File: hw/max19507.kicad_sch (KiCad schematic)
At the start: 43 parts, among them U8 THS4522, U9 MAX19517

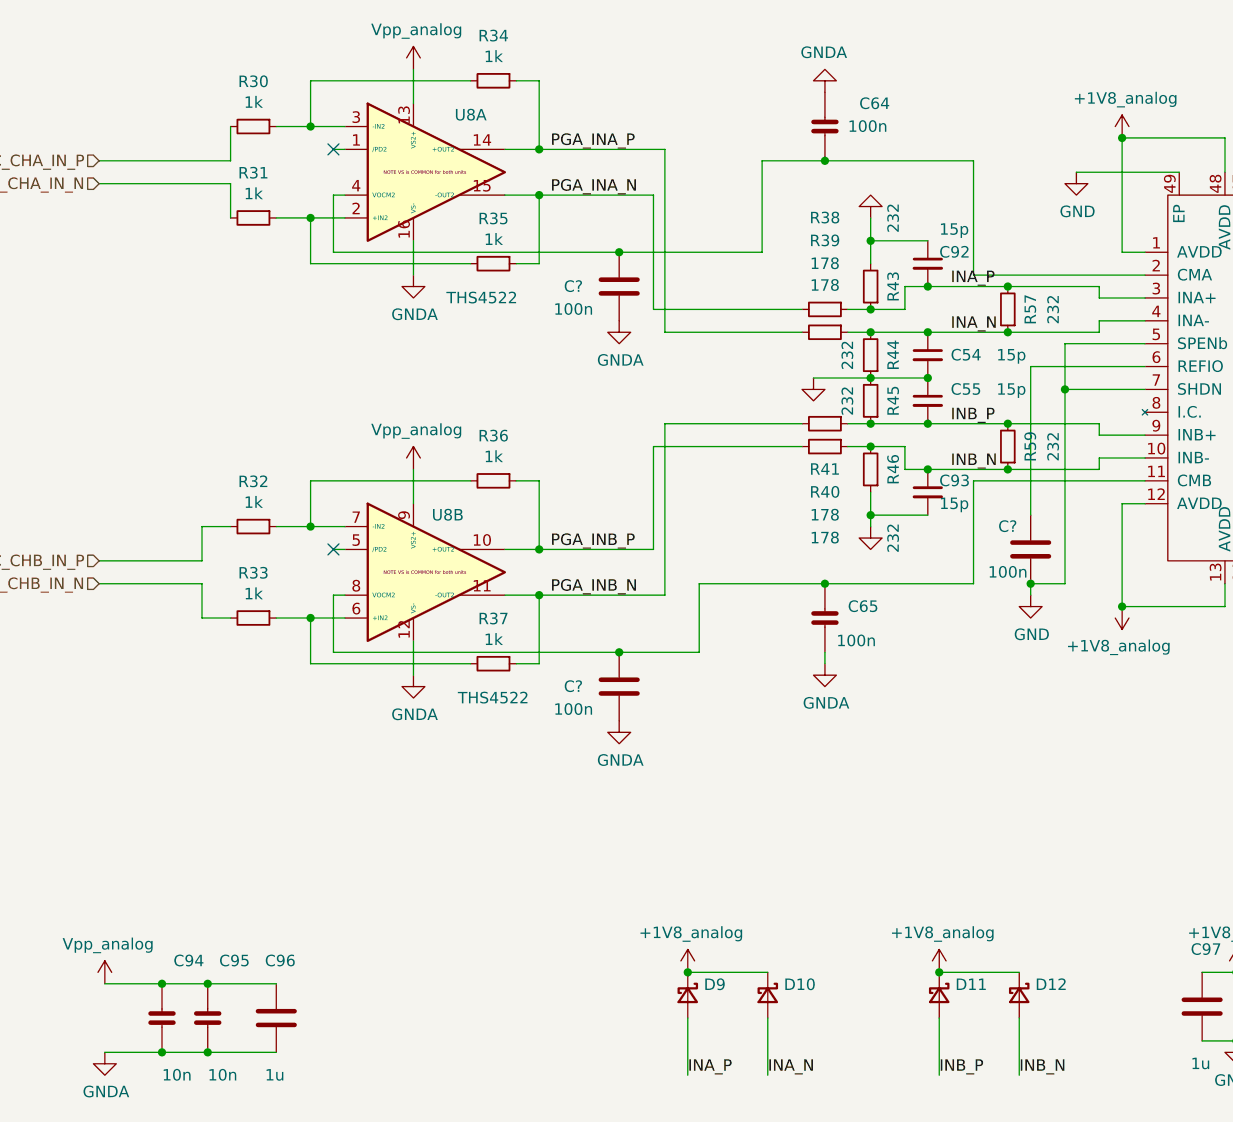
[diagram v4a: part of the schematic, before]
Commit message: standardized resistor/capacitor values
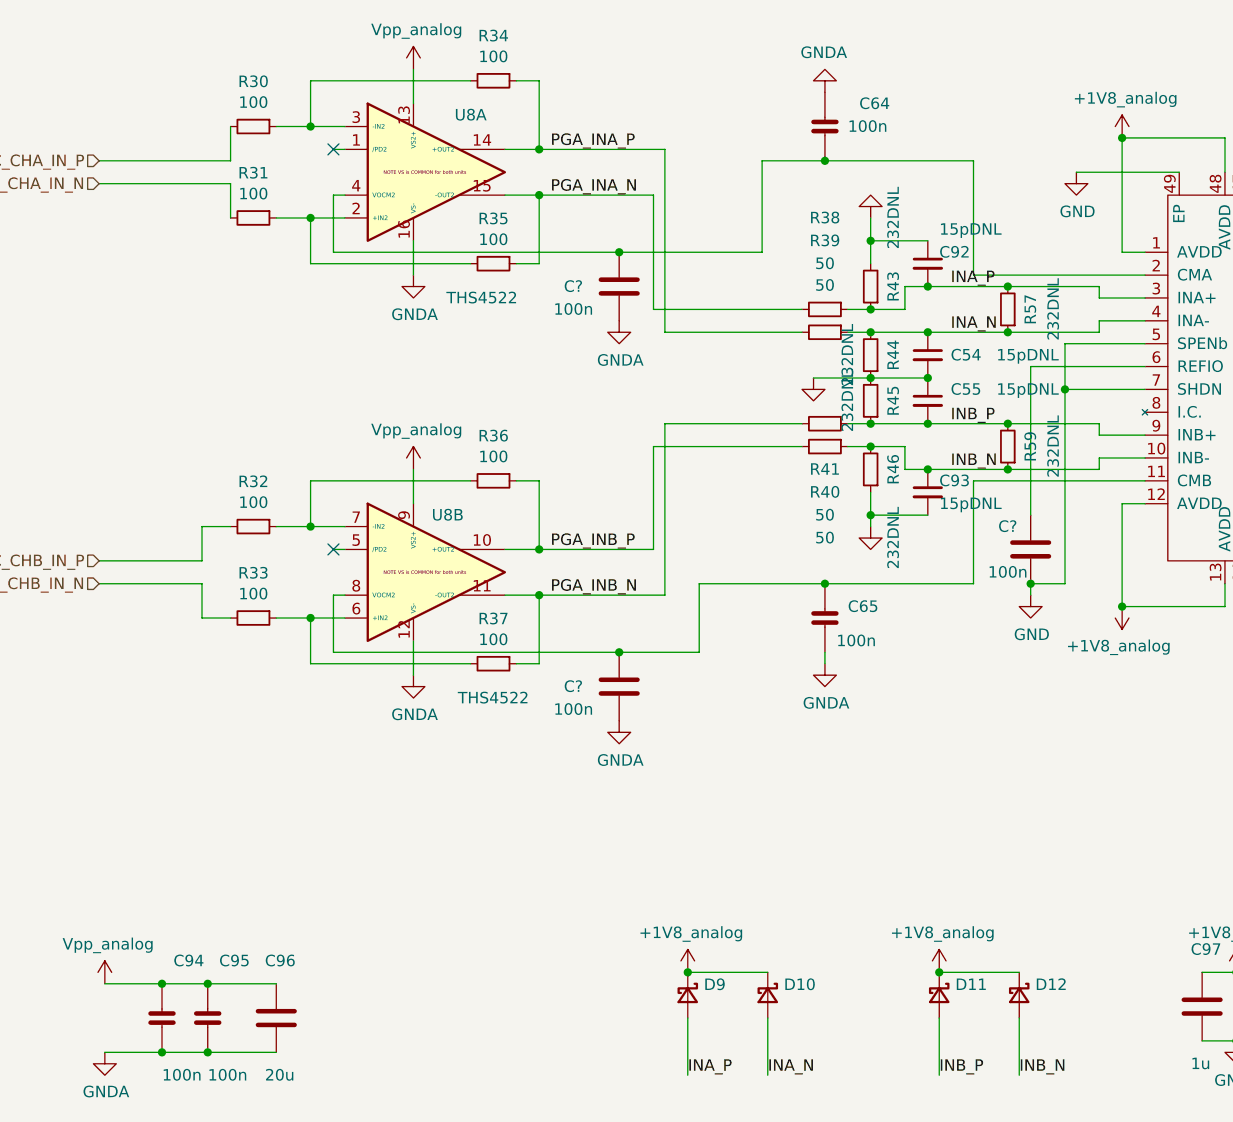
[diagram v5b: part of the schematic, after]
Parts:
- C54, C55, C92, C93: value 15p -> 15pDNL
- C94, C95: value 10n -> 100n
- C96: value 1u -> 20u
- R30, R31, R32, R33, R34, R35, R36, R37: value 1k -> 100
- R38, R39, R40, R41: value 178 -> 50
- R43, R44, R45, R46, R57, R59: value 232 -> 232DNL
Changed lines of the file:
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@@
       (effects (font (size 1.27 1.27)))
     )
-    (property "Value" "232" (at 191.77 78.74 90)
+    (property "Value" "232DNL" (at 191.77 78.74 90)
       (effects (font (size 1.27 1.27)))
     )
@@
       (effects (font (size 1.27 1.27)))
     )
-    (property "Value" "232" (at 191.77 93.98 90)
+    (property "Value" "232DNL" (at 191.77 93.98 90)
       (effects (font (size 1.27 1.27)))
     )
@@
       (effects (font (size 1.27 1.27)) (justify left))
     )
-    (property "Value" "15p" (at 179.07 100.33 0)
+    (property "Value" "15pDNL" (at 179.07 100.33 0)
       (effects (font (size 1.27 1.27)) (justify left))
     )
@@
       (effects (font (size 1.27 1.27)) (justify left))
     )
-    (property "Value" "15p" (at 179.07 69.85 0)
+    (property "Value" "15pDNL" (at 179.07 69.85 0)
       (effects (font (size 1.27 1.27)) (justify left))
     )
@@
       (effects (font (size 1.27 1.27)) (justify left))
     )
-    (property "Value" "10n" (at 92.71 163.83 0)
+    (property "Value" "100n" (at 92.71 163.83 0)
       (effects (font (size 1.27 1.27)) (justify left))
     )
@@
       (effects (font (size 1.27 1.27)) (justify left))
     )
-    (property "Value" "10n" (at 97.79 163.83 0)
+    (property "Value" "100n" (at 97.79 163.83 0)
       (effects (font (size 1.27 1.27)) (justify left))
     )
@@
       (effects (font (size 1.27 1.27)) (justify left))
     )
-    (property "Value" "1u" (at 104.14 163.83 0)
+    (property "Value" "20u" (at 104.14 163.83 0)
       (effects (font (size 1.27 1.27)) (justify left))
     )
@@
       (effects (font (size 1.27 1.27)))
     )
-    (property "Value" "232" (at 168.91 83.82 90)
+    (property "Value" "232DNL" (at 168.91 83.82 90)
       (effects (font (size 1.27 1.27)))
     )
@@
       (effects (font (size 1.27 1.27)))
     )
-    (property "Value" "232" (at 173.99 68.58 90)
+    (property "Value" "232DNL" (at 173.99 68.58 90)
       (effects (font (size 1.27 1.27)))
     )
@@
       (effects (font (size 1.27 1.27)))
     )
-    (property "Value" "232" (at 168.91 88.9 90)
+    (property "Value" "232DNL" (at 168.91 88.9 90)
       (effects (font (size 1.27 1.27)))
     )
@@
       (effects (font (size 1.27 1.27)))
     )
-    (property "Value" "232" (at 173.99 104.14 90)
+    (property "Value" "232DNL" (at 173.99 104.14 90)
       (effects (font (size 1.27 1.27)))
     )
@@
       (effects (font (size 1.27 1.27)))
     )
-    (property "Value" "178" (at 166.37 76.073 90)
+    (property "Value" "50" (at 166.37 76.073 90)
       (effects (font (size 1.27 1.27)))
     )
@@
       (effects (font (size 1.27 1.27)) (justify left))
     )
-    (property "Value" "15p" (at 185.42 83.82 0)
+    (property "Value" "15pDNL" (at 185.42 83.82 0)
       (effects (font (size 1.27 1.27)) (justify left))
     )
@@
       (effects (font (size 1.27 1.27)))
     )
-    (property "Value" "178" (at 166.37 73.66 90)
+    (property "Value" "50" (at 166.37 73.66 90)
       (effects (font (size 1.27 1.27)))
     )
@@
       (effects (font (size 1.27 1.27)))
     )
-    (property "Value" "1k" (at 129.54 50.673 90)
+    (property "Value" "100" (at 129.54 50.673 90)
       (effects (font (size 1.27 1.27)))
     )
@@
       (effects (font (size 1.27 1.27)))
     )
-    (property "Value" "1k" (at 102.87 55.753 90)
+    (property "Value" "100" (at 102.87 55.753 90)
       (effects (font (size 1.27 1.27)))
     )
@@
       (effects (font (size 1.27 1.27)))
     )
-    (property "Value" "1k" (at 102.87 65.913 90)
+    (property "Value" "100" (at 102.87 65.913 90)
       (effects (font (size 1.27 1.27)))
     )
@@
       (effects (font (size 1.27 1.27)))
     )
-    (property "Value" "1k" (at 129.54 70.993 90)
+    (property "Value" "100" (at 129.54 70.993 90)
       (effects (font (size 1.27 1.27)))
     )
@@
       (effects (font (size 1.27 1.27)))
     )
-    (property "Value" "178" (at 166.37 104.14 90)
+    (property "Value" "50" (at 166.37 104.14 90)
       (effects (font (size 1.27 1.27)))
     )
@@
       (effects (font (size 1.27 1.27)) (justify left))
     )
-    (property "Value" "15p" (at 185.42 87.63 0)
+    (property "Value" "15pDNL" (at 185.42 87.63 0)
       (effects (font (size 1.27 1.27)) (justify left))
     )
@@
       (effects (font (size 1.27 1.27)))
     )
-    (property "Value" "178" (at 166.37 101.6 90)
+    (property "Value" "50" (at 166.37 101.6 90)
       (effects (font (size 1.27 1.27)))
     )
@@
       (effects (font (size 1.27 1.27)))
     )
-    (property "Value" "1k" (at 129.54 95.123 90)
+    (property "Value" "100" (at 129.54 95.123 90)
       (effects (font (size 1.27 1.27)))
     )
@@
       (effects (font (size 1.27 1.27)))
     )
-    (property "Value" "1k" (at 102.87 100.203 90)
+    (property "Value" "100" (at 102.87 100.203 90)
       (effects (font (size 1.27 1.27)))
     )
@@
       (effects (font (size 1.27 1.27)))
     )
-    (property "Value" "1k" (at 102.87 110.363 90)
+    (property "Value" "100" (at 102.87 110.363 90)
       (effects (font (size 1.27 1.27)))
     )
@@
       (effects (font (size 1.27 1.27)))
     )
-    (property "Value" "1k" (at 129.54 115.443 90)
-      (effects (font (size 1.27 1.27)))
-    )
+    (property "Value" "100" (at 129.54 115.443 90)
+      (effects (font (size 1.27 1.27)))
+    )

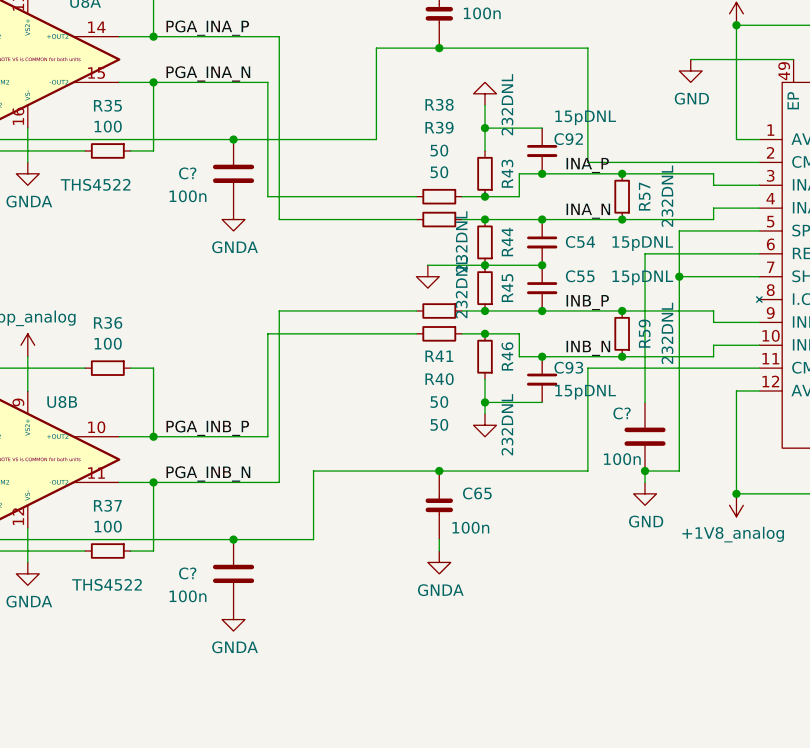
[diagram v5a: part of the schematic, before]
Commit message: Added trion top-sheet as sub-sheet to usbadc project
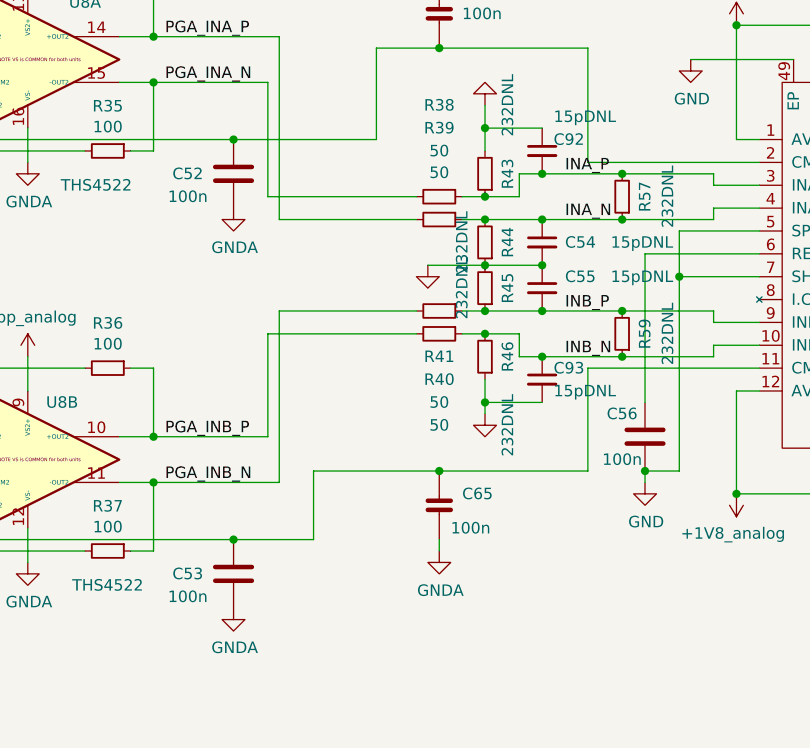
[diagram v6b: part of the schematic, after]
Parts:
- gave numbers to parts that had none: 3
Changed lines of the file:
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@@
           (reference "#PWR0145") (unit 1)
-        )
-        (path "/7c8a1f8d-8834-4c9b-aaae-1f231e9b09a1/00000000-0000-0000-0000-000060b16d71"
-          (reference "#PWR?") (unit 1)
-        )
-        (path "/7c8a1f8d-8834-4c9b-aaae-1f231e9b09a1/00000000-0000-0000-0000-00006086f2e3"
-          (reference "#PWR?") (unit 1)
         )
       )
@@
           (reference "C96") (unit 1)
         )
-        (path "/7c8a1f8d-8834-4c9b-aaae-1f231e9b09a1/00000000-0000-0000-0000-000060b16d71"
-          (reference "C?") (unit 1)
-        )
       )
     )
@@
           (reference "C97") (unit 1)
         )
-        (path "/7c8a1f8d-8834-4c9b-aaae-1f231e9b09a1/00000000-0000-0000-0000-000060b16d71"
-          (reference "C?") (unit 1)
-        )
       )
     )
@@
           (reference "#PWR0148") (unit 1)
         )
-        (path "/7c8a1f8d-8834-4c9b-aaae-1f231e9b09a1/00000000-0000-0000-0000-000060b16d71"
-          (reference "#PWR?") (unit 1)
-        )
-        (path "/7c8a1f8d-8834-4c9b-aaae-1f231e9b09a1/00000000-0000-0000-0000-00006086f2e3"
-          (reference "#PWR?") (unit 1)
-        )
       )
     )
@@
           (reference "#PWR0139") (unit 1)
         )
-        (path "/7c8a1f8d-8834-4c9b-aaae-1f231e9b09a1/00000000-0000-0000-0000-000060b16d71"
-          (reference "#PWR?") (unit 1)
-        )
-        (path "/7c8a1f8d-8834-4c9b-aaae-1f231e9b09a1/00000000-0000-0000-0000-00006086f2e3"
-          (reference "#PWR?") (unit 1)
-        )
       )
     )
@@
         (path "/7c8a1f8d-8834-4c9b-aaae-1f231e9b09a1/00000000-0000-0000-0000-0000612b1274"
           (reference "#PWR0122") (unit 1)
-        )
-        (path "/7c8a1f8d-8834-4c9b-aaae-1f231e9b09a1/00000000-0000-0000-0000-000060b16d71"
-          (reference "#PWR?") (unit 1)
-        )
-        (path "/7c8a1f8d-8834-4c9b-aaae-1f231e9b09a1/00000000-0000-0000-0000-00006086f2e3"
-          (reference "#PWR?") (unit 1)
         )
       )
@@
   (symbol (lib_id "fmc:100nF_603") (at 143.51 76.2 180) (unit 1)
     (in_bom yes) (on_board yes) (dnp no)
-    (property "Reference" "C?" (at 138.43 76.2 0)
+    (property "Reference" "C52" (at 138.43 76.2 0)
       (effects (font (size 1.27 1.27)))
     )
@@
     (instances
       (project "usbadc"
-        (path "/7c8a1f8d-8834-4c9b-aaae-1f231e9b09a1/00000000-0000-0000-0000-000060b16d71"
-          (reference "C?") (unit 1)
-        )
-        (path "/7c8a1f8d-8834-4c9b-aaae-1f231e9b09a1/00000000-0000-0000-0000-00006086f2e3"
-          (reference "C?") (unit 1)
-        )
         (path "/7c8a1f8d-8834-4c9b-aaae-1f231e9b09a1/00000000-0000-0000-0000-0000612b1274"
           (reference "C52") (unit 1)
@@
   (symbol (lib_id "fmc:100nF_603") (at 143.51 120.65 180) (unit 1)
     (in_bom yes) (on_board yes) (dnp no)
-    (property "Reference" "C?" (at 138.43 120.65 0)
+    (property "Reference" "C53" (at 138.43 120.65 0)
       (effects (font (size 1.27 1.27)))
     )
@@
     (instances
       (project "usbadc"
-        (path "/7c8a1f8d-8834-4c9b-aaae-1f231e9b09a1/00000000-0000-0000-0000-000060b16d71"
-          (reference "C?") (unit 1)
-        )
-        (path "/7c8a1f8d-8834-4c9b-aaae-1f231e9b09a1/00000000-0000-0000-0000-00006086f2e3"
-          (reference "C?") (unit 1)
-        )
         (path "/7c8a1f8d-8834-4c9b-aaae-1f231e9b09a1/00000000-0000-0000-0000-0000612b1274"
           (reference "C53") (unit 1)
@@
           (reference "#PWR0136") (unit 1)
         )
-        (path "/7c8a1f8d-8834-4c9b-aaae-1f231e9b09a1/00000000-0000-0000-0000-000060b16d71"
-          (reference "#PWR?") (unit 1)
-        )
-        (path "/7c8a1f8d-8834-4c9b-aaae-1f231e9b09a1/00000000-0000-0000-0000-00006086f2e3"
-          (reference "#PWR?") (unit 1)
-        )
       )
     )
@@
           (reference "#PWR0137") (unit 1)
         )
-        (path "/7c8a1f8d-8834-4c9b-aaae-1f231e9b09a1/00000000-0000-0000-0000-000060b16d71"
-          (reference "#PWR?") (unit 1)
-        )
-        (path "/7c8a1f8d-8834-4c9b-aaae-1f231e9b09a1/00000000-0000-0000-0000-00006086f2e3"
-          (reference "#PWR?") (unit 1)
-        )
       )
     )
@@
           (reference "#PWR0135") (unit 1)
         )
-        (path "/7c8a1f8d-8834-4c9b-aaae-1f231e9b09a1/00000000-0000-0000-0000-000060b16d71"
-          (reference "#PWR?") (unit 1)
-        )
-        (path "/7c8a1f8d-8834-4c9b-aaae-1f231e9b09a1/00000000-0000-0000-0000-00006086f2e3"
-          (reference "#PWR?") (unit 1)
-        )
       )
     )
@@
           (reference "C62") (unit 1)
         )
-        (path "/7c8a1f8d-8834-4c9b-aaae-1f231e9b09a1/00000000-0000-0000-0000-000060b16d71"
-          (reference "C?") (unit 1)
-        )
       )
     )
@@
           (reference "C61") (unit 1)
         )
-        (path "/7c8a1f8d-8834-4c9b-aaae-1f231e9b09a1/00000000-0000-0000-0000-000060b16d71"
-          (reference "C?") (unit 1)
-        )
       )
     )
@@
           (reference "#PWR0140") (unit 1)
         )
-        (path "/7c8a1f8d-8834-4c9b-aaae-1f231e9b09a1/00000000-0000-0000-0000-000060b16d71"
-          (reference "#PWR?") (unit 1)
-        )
-        (path "/7c8a1f8d-8834-4c9b-aaae-1f231e9b09a1/00000000-0000-0000-0000-00006086f2e3"
-          (reference "#PWR?") (unit 1)
-        )
       )
     )
@@
           (reference "#PWR0141") (unit 1)
         )
-        (path "/7c8a1f8d-8834-4c9b-aaae-1f231e9b09a1/00000000-0000-0000-0000-000060b16d71"
-          (reference "#PWR?") (unit 1)
-        )
-        (path "/7c8a1f8d-8834-4c9b-aaae-1f231e9b09a1/00000000-0000-0000-0000-00006086f2e3"
-          (reference "#PWR?") (unit 1)
-        )
       )
     )
@@
           (reference "#PWR0142") (unit 1)
         )
-        (path "/7c8a1f8d-8834-4c9b-aaae-1f231e9b09a1/00000000-0000-0000-0000-000060b16d71"
-          (reference "#PWR?") (unit 1)
-        )
-        (path "/7c8a1f8d-8834-4c9b-aaae-1f231e9b09a1/00000000-0000-0000-0000-00006086f2e3"
-          (reference "#PWR?") (unit 1)
-        )
       )
     )
@@
   (symbol (lib_id "fmc:100nF_603") (at 189.23 105.41 180) (unit 1)
     (in_bom yes) (on_board yes) (dnp no)
-    (property "Reference" "C?" (at 186.69 102.87 0)
+    (property "Reference" "C56" (at 186.69 102.87 0)
       (effects (font (size 1.27 1.27)))
     )
@@
     (instances
       (project "usbadc"
-        (path "/7c8a1f8d-8834-4c9b-aaae-1f231e9b09a1/00000000-0000-0000-0000-000060b16d71"
-          (reference "C?") (unit 1)
-        )
-        (path "/7c8a1f8d-8834-4c9b-aaae-1f231e9b09a1/00000000-0000-0000-0000-00006086f2e3"
-          (reference "C?") (unit 1)
-        )
         (path "/7c8a1f8d-8834-4c9b-aaae-1f231e9b09a1/00000000-0000-0000-0000-0000612b1274"
           (reference "C56") (unit 1)
